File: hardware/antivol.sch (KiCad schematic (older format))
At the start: 18 parts, among them J1 Conn_01x02, J2 Conn_01x06, J3 Conn_01x07, U1 ESP32-WROOM-32D, U2 MPU-6050, U3 SY8089AAAC(SOT23-5)

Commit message: Add charger
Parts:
- removed C4: 0.1µF, Capacitor_SMD:C_0603_1608Metric_Pad1.05x0.95mm_HandSolder, symbol Device:C
- removed J3: Conn_01x07, Connector_PinHeader_2.54mm:PinHeader_2x04_P2.54mm_Vertical, symbol Connector_Generic:Conn_02x04_Odd_Even
- removed U1: ESP32-WROOM-32D, RF_Module:ESP32-WROOM-32, symbol RF_Module:ESP32-WROOM-32D
- removed U2: MPU-6050, Sensor_Motion:InvenSense_QFN-24_4x4mm_P0.5mm, symbol Sensor_Motion:MPU-6050
- added D1, D3: SS14, Diode_SMD:D_SMA, symbol Device:D_Schottky
- added D2: LED, Diode_SMD:D_0603_1608Metric, symbol Device:LED
- added J3: Conn_01x02, Connector_PinHeader_2.54mm:PinHeader_1x02_P2.54mm_Vertical, symbol Connector_Generic:Conn_01x02
- added Q1, Q2: AO3401A, Package_TO_SOT_SMD:SOT-23, symbol Device:Q_PMOS_GSD
- added Q3: 2N7002, Package_TO_SOT_SMD:SOT-23, symbol Transistor_FET:2N7002
- added R6, R7: 2.2k, Resistor_SMD:R_0603_1608Metric, symbol Device:R
- added R8, R9: 10k, Resistor_SMD:R_0603_1608Metric, symbol Device:R
- added TP1, TP2, TP3, TP4, TP5, TP6, TP7: TestPoint, TestPoint:TestPoint_Pad_D1.5mm, symbol Connector:TestPoint
- added U1: ESP-WROOM-32, OLIMEX_Cases-FP:ESP-WROOM-32_MODULE, symbol OLIMEX_Cases:ESP-WROOM-32
- added U2: TP4054 (SOT23-5), Package_TO_SOT_SMD:SOT-23-5, symbol OLIMEX_IC:BL4054B-42TPRN(SOT23-5)
- added U4: KXTJ3-1057, Package_LGA:LGA-12_2x2mm_P0.5mm, symbol components:KXTJ3-1057
- C1: value 2.2nF -> 47µF/6.3V; footprint Capacitor_SMD:C_0603_1608Metric_Pad1.05x0.95mm_HandSolder -> Capacitor_SMD:C_0805_2012Metric
- C2, C3: footprint Capacitor_SMD:C_0603_1608Metric_Pad1.05x0.95mm_HandSolder -> Capacitor_SMD:C_0603_1608Metric
- C6, C7: footprint Capacitor_SMD:C_0805_2012Metric_Pad1.15x1.40mm_HandSolder -> Capacitor_SMD:C_0805_2012Metric
- L1: value 2.2µH/1.5A -> 15µH/450mA - NLC453232T-150K-PF; footprint Inductor_SMD:L_Wuerth_HCI-5040 -> Inductor_SMD:L_1812_4532Metric
- R1, R2, R3, R4, R5: footprint Resistor_SMD:R_0603_1608Metric_Pad1.05x0.95mm_HandSolder -> Resistor_SMD:R_0603_1608Metric
- U3: footprint Package_TO_SOT_SMD:SOT-23-5_HandSoldering -> Package_TO_SOT_SMD:SOT-23-5
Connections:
- net labels added: +5V_USB, ADC, ADC_EN, GSM_VBAT
- wire segments 78 -> 127
- no-connect marks 15 -> 22
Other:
- moved on the sheet: C2, C3, C6, C7, J2, L1, R1, R2, R3, R4, R5, U3

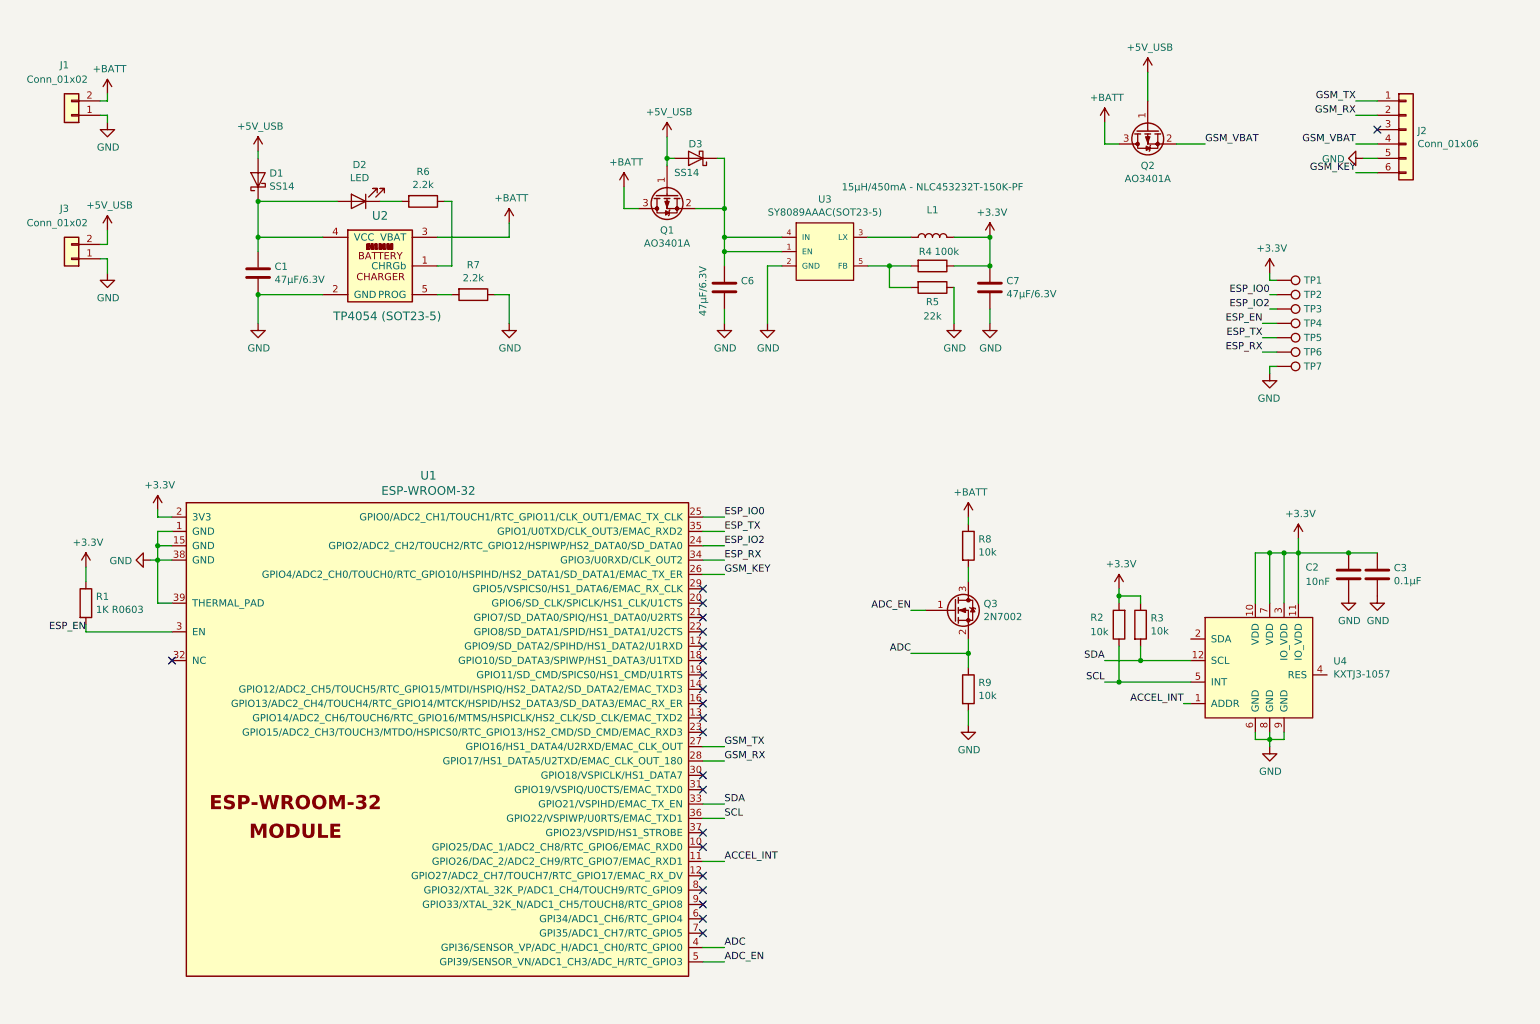
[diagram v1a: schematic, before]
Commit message: final without usb
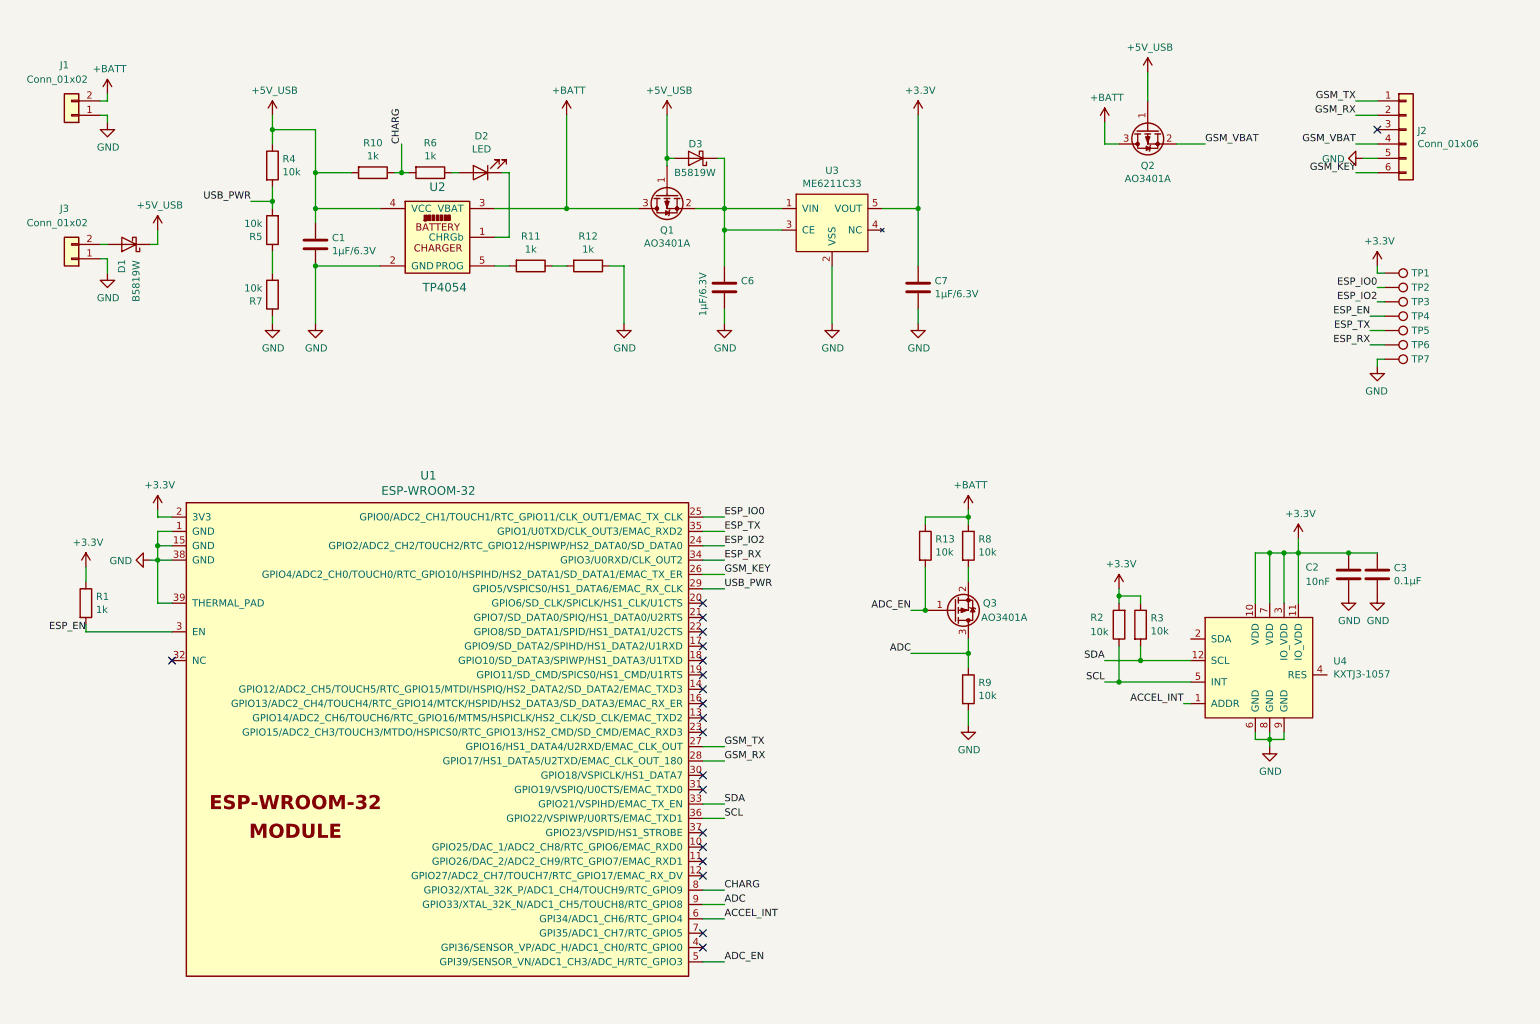
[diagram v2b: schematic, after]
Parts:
- removed L1: 15µH/450mA - NLC453232T-150K-PF, Inductor_SMD:L_1812_4532Metric, symbol Device:L
- removed Q3: 2N7002, Package_TO_SOT_SMD:SOT-23, symbol Transistor_FET:2N7002
- removed U3: SY8089AAAC(SOT23-5), Package_TO_SOT_SMD:SOT-23-5, symbol OLIMEX_IC:SY8009AAAC(SOT23-5)
- added Q3: AO3401A, Package_TO_SOT_SMD:SOT-23, symbol Device:Q_PMOS_GSD
- added R10, R11, R12: 1k, Resistor_SMD:R_0603_1608Metric, symbol Device:R
- added R13: 10k, Resistor_SMD:R_0603_1608Metric, symbol Device:R
- added U3: ME6211C33, Package_TO_SOT_SMD:SOT-23-5, symbol components:ME6211C33
- C1, C6, C7: value 47µF/6.3V -> 1µF/6.3V; footprint Capacitor_SMD:C_0805_2012Metric -> Capacitor_SMD:C_0603_1608Metric; LCSC (none) -> C15849
- C2: LCSC (none) -> C57112
- C3: LCSC (none) -> C14663
- D1, D3: value SS14 -> B5819W; footprint Diode_SMD:D_SMA -> Diode_SMD:D_SOD-123; LCSC (none) -> C8598
- D2: LCSC (none) -> C72038
- Q1, Q2: LCSC (none) -> C15127
- R1: value 1K R0603 -> 1k; LCSC (none) -> C21190
- R2, R3, R8, R9: LCSC (none) -> C25804
- R4: value 100k -> 10k; LCSC (none) -> C25804
- R5: value 22k -> 10k; LCSC (none) -> C25804
- R6: value 2.2k -> 1k; LCSC (none) -> C21190
- R7: value 2.2k -> 10k; LCSC (none) -> C25804
- U2: value TP4054 (SOT23-5) -> TP4054; LCSC (none) -> C32574
- U4: LCSC (none) -> C442603
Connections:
- net +3V3: now also U3.5 (VOUT); no longer R4.1
- net +5V_USB: now also C1.1, D1.1 (K), R4.1, U2.4 (VCC), R10.2; no longer D1.2 (A), J3.2 (Pin_2)
- net +BATT: now also R13.1
- net ACCEL_INT: now also U1.6 (GPI34/ADC1_CH6/RTC_GPIO4); no longer U1.11 (GPIO26/DAC_2/ADC2_CH9/RTC_GPIO7/EMAC_RXD1)
- net ADC: now also U1.9 (GPIO33/XTAL_32K_N/ADC1_CH5/TOUCH8/RTC_GPIO8), Q3.3 (D); no longer U1.4 (GPI36/SENSOR_VP/ADC_H/ADC1_CH0/RTC_GPIO0)
- net ADC_EN: now also Q3.1 (G), R13.2
- net GND: now also R12.1, U3.2 (VSS); no longer R5.1
- net USB_PWR: now reaches U1.29 (GPIO5/VSPICS0/HS1_DATA6/EMAC_RX_CLK)
- net USB_PWR: now also R4.2, R5.2
- net CHARG: now reaches U1.8 (GPIO32/XTAL_32K_P/ADC1_CH4/TOUCH9/RTC_GPIO9)
- net CHARG: now also R6.2, R10.1
- net at C6.1, D3.1 (K), Q1.2 (S): now also U3.1 (VIN), U3.3 (CE)
- net at R8.2: now also Q3.2 (S)
- net at U2.1 (CHRGb): now also D2.1 (K); no longer R6.1
- net at U2.5 (PROG): now also R11.2; no longer R7.2
- new net: D1.2 (A), J3.2 (Pin_2)
- new net: D2.2 (A), R6.1
- new net: R5.1, R7.2
- new net: R11.1, R12.2
- no-connect marks 22 -> 20
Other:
- moved on the sheet: C1, C7, D1, D2, R6, TP1, TP2, TP3, TP4, TP5, TP6, TP7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

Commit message: cp2102
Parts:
- removed J3: Conn_01x02, Connector_PinHeader_2.54mm:PinHeader_1x02_P2.54mm_Vertical, symbol Connector_Generic:Conn_01x02
- removed R12: 1k, Resistor_SMD:R_0603_1608Metric, symbol Device:R
- removed R7: 10k, Resistor_SMD:R_0603_1608Metric, symbol Device:R
- removed TP1, TP2, TP3, TP4, TP5, TP6, TP7: TestPoint, TestPoint:TestPoint_Pad_D1.5mm, symbol Connector:TestPoint
- added C10, C8: 0.1µF, Capacitor_SMD:C_0603_1608Metric, symbol Device:C
- added C4: 1nF, Capacitor_SMD:C_0603_1608Metric, symbol Device:C
- added C5, C9: 10µF/25V, Capacitor_SMD:C_0805_2012Metric, symbol Device:C
- added J4: USB_B_Micro, Connector_USB:USB_Micro-B_Molex-105017-0001, symbol Connector:USB_B_Micro
- added Q4, Q5: S8050, Package_TO_SOT_SMD:SOT-23, symbol Device:Q_NPN_BEC
- added R14: 470, Resistor_SMD:R_0603_1608Metric, symbol Device:R
- added R15, R16: 12k, Resistor_SMD:R_0603_1608Metric, symbol Device:R
- added U5: USBLC6-2SC6, Package_TO_SOT_SMD:SOT-23-6_Handsoldering, symbol Power_Protection:USBLC6-2SC6
- added U6: CP2102N-A01-GQFN28, Package_DFN_QFN:QFN-28-1EP_5x5mm_P0.5mm_EP3.35x3.35mm, symbol Interface_USB:CP2102N-A01-GQFN28
- R11: value 1k -> 2.2k; LCSC C21190 -> C4190
- R5: value 10k -> 22k; LCSC C25804 -> C31850
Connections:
- net ESP_IO2 is gone; now on net GSM_KEY: U1.24 (GPIO2/ADC2_CH2/TOUCH2/RTC_GPIO12/HSPIWP/HS2_DATA0/SD_DATA0)
- net +3V3: now also C10.1, C9.2, U6.6 (VDD), U6.7 (REGIN)
- net +5V_USB: now also C5.2, C8.1, U6.8 (VBUS)
- net ACCEL_INT: now also U1.4 (GPI36/SENSOR_VP/ADC_H/ADC1_CH0/RTC_GPIO0); no longer U1.6 (GPI34/ADC1_CH6/RTC_GPIO4)
- net CHARG: now also U1.14 (GPIO12/ADC2_CH5/TOUCH5/RTC_GPIO15/MTDI/HSPIQ/HS2_DATA2/SD_DATA2/EMAC_TXD3); no longer U1.8 (GPIO32/XTAL_32K_P/ADC1_CH4/TOUCH9/RTC_GPIO9)
- net ESP_EN: now also C4.2, Q4.3 (C)
- net ESP_IO0: now also Q5.3 (C)
- net ESP_RX: now also R14.1
- net ESP_TX: now also U6.25 (RXD)
- net GND: now also R11.1, R5.1, C10.2, C4.1, C5.1, C8.2, C9.1, J4.5 (GND), J4.6 (Shield), U5.2 (GND), U6.29 (GND), U6.3 (GND)
- net GSM_KEY: no longer U1.26 (GPIO4/ADC2_CH0/TOUCH0/RTC_GPIO10/HSPIHD/HS2_DATA1/SD_DATA1/EMAC_TX_ER)
- net USB_PWR: now also U1.13 (GPIO14/ADC2_CH6/TOUCH6/RTC_GPIO16/MTMS/HSPICLK/HS2_CLK/SD_CLK/EMAC_TXD2); no longer U1.29 (GPIO5/VSPICS0/HS1_DATA6/EMAC_RX_CLK)
- net at D1.2 (A): now also J4.1 (VBUS), U5.5 (VBUS)
- new net: Q4.2 (E), R16.1, U6.24 (~RTS)
- new net: R14.2, U6.26 (TXD)
- new net: Q5.2 (E), R15.1, U6.28 (~DTR)
- new net: Q5.1 (B), R16.2
- new net: Q4.1 (B), R15.2
- new net USB_D+: J4.3 (D+), U5.3 (IO2), U5.4 (IO2), U6.4 (D+)
- new net USB_D-: J4.2 (D-), U5.1 (IO1), U5.6 (IO1), U6.5 (D-)
- no-connect marks 20 -> 39
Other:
- moved on the sheet: C1, C2, C3, C6, C7, D1, D2, D3, J2, Q1, Q2, Q3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

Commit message: v1
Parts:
- removed C5: 10µF/25V, Capacitor_SMD:C_0805_2012Metric, symbol Device:C
- removed C8: 0.1µF, Capacitor_SMD:C_0603_1608Metric, symbol Device:C
- removed U3: ME6211C33, Package_TO_SOT_SMD:SOT-23-5, symbol components:ME6211C33
- removed U5: USBLC6-2SC6, Package_TO_SOT_SMD:SOT-23-6_Handsoldering, symbol Power_Protection:USBLC6-2SC6
- removed U6: CP2102N-A01-GQFN28, Package_DFN_QFN:QFN-28-1EP_5x5mm_P0.5mm_EP3.35x3.35mm, symbol Interface_USB:CP2102N-A01-GQFN28
- added C5, C8: 12pF, Capacitor_SMD:C_0603_1608Metric, symbol Device:C_Small
- added R12: 10k, Resistor_SMD:R_0603_1608Metric, symbol Device:R
- added R7: 470, Resistor_SMD:R_0603_1608Metric, symbol Device:R
- added U3: XC6206P332, Package_TO_SOT_SMD:SOT-23, symbol Regulator_Linear:AP1117-33
- added U5: CH340G, Package_SO:SOIC-16_3.9x9.9mm_P1.27mm, symbol Interface_USB:CH340G
- added Y1: 12MHz, Crystal:Crystal_SMD_3225-4Pin_3.2x2.5mm, symbol Device:Crystal_GND24_Small
- C2: value 10nF -> 0.1µF; LCSC C57112 -> C14663
- R1: value 1k -> 2.2k; LCSC C21190 -> C4190
- R13: value 10k -> 22k; LCSC C25804 -> C31850
- R15: value 12k -> 10k; LCSC C22790 -> C25804
- R16: value 12k -> 22k; LCSC C22790 -> C31850
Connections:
- net +3V3: now also R1.2, U3.2 (VO), U5.16 (VCC), U5.4 (V3); no longer R1.1
- net +5V_USB: no longer Q2.1 (G)
- net +BATT: now also Q2.2 (S), R13.2, R16.2; no longer Q2.3 (D), R13.1
- net ACCEL_INT: now also U4.5 (INT); no longer U4.1 (ADDR)
- net ADC_EN: now also R16.1, U1.8 (GPIO32/XTAL_32K_P/ADC1_CH4/TOUCH9/RTC_GPIO9); no longer R13.2, U1.5 (GPI39/SENSOR_VN/ADC1_CH3/ADC_H/RTC_GPIO3)
- net CHARG: now also U1.13 (GPIO14/ADC2_CH6/TOUCH6/RTC_GPIO16/MTMS/HSPICLK/HS2_CLK/SD_CLK/EMAC_TXD2); no longer U1.14 (GPIO12/ADC2_CH5/TOUCH5/RTC_GPIO15/MTDI/HSPIQ/HS2_DATA2/SD_DATA2/EMAC_TXD3)
- net ESP_EN: now also R1.1; no longer R1.2
- net ESP_RX: now also R7.1; no longer R14.1
- net ESP_TX: now also R14.1
- net GND: now also U4.1 (ADDR), U4.4 (RES), C5.2, C8.1, U3.1 (GND), U5.1 (GND), Y1.2, Y1.4
- net GSM_VBAT: now also Q2.3 (D); no longer Q2.2 (S)
- net SCL: now also U4.12 (SCL); no longer U4.5 (INT)
- net SDA: now also U4.2 (SDA); no longer U4.12 (SCL)
- net USB_D+: now also U5.5 (UD+)
- net USB_D-: now also U5.6 (UD-)
- net USB_PWR: now also U1.10 (GPIO25/DAC_1/ADC2_CH8/RTC_GPIO6/EMAC_RXD0); no longer U1.13 (GPIO14/ADC2_CH6/TOUCH6/RTC_GPIO16/MTMS/HSPICLK/HS2_CLK/SD_CLK/EMAC_TXD2)
- net at C6.1, D3.1 (K), Q1.2 (S): now also U3.3 (VI)
- net at Q4.2 (E): now also R15.1, U5.14 (~RTS); no longer R16.1
- net at R14.2: now also U5.3 (RXD)
- net at Q5.2 (E): now also R12.1, U5.13 (~DTR); no longer R15.1
- net at Q5.1 (B): now also R15.2; no longer R16.2
- net at Q4.1 (B): now also R12.2; no longer R15.2
- new net: R7.2, U5.2 (TXD)
- new net: C5.1, U5.7 (XI), Y1.1
- new net: C8.2, U5.8 (XO), Y1.3
- new net GSM_PWR: Q2.1 (G), R13.1, U1.14 (GPIO12/ADC2_CH5/TOUCH5/RTC_GPIO15/MTDI/HSPIQ/HS2_DATA2/SD_DATA2/EMAC_TXD3)
- no-connect marks 39 -> 26
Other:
- moved on the sheet: C10, C9, D1, Q4, Q5, R14, R2, R3
